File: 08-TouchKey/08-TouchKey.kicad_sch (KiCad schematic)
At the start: 21 parts, among them J1 AudioJack3, P1 TouchPaddles, P2 TouchPaddles, P3 TouchPaddles, P4 TouchPaddles, P5 TouchPaddles, P6 TouchPaddles, Q1 Q_Dual_PMOS_S1G1D2S2G2D1, U1 AT42QT1011-TSHR, U2 AT42QT1011-TSHR

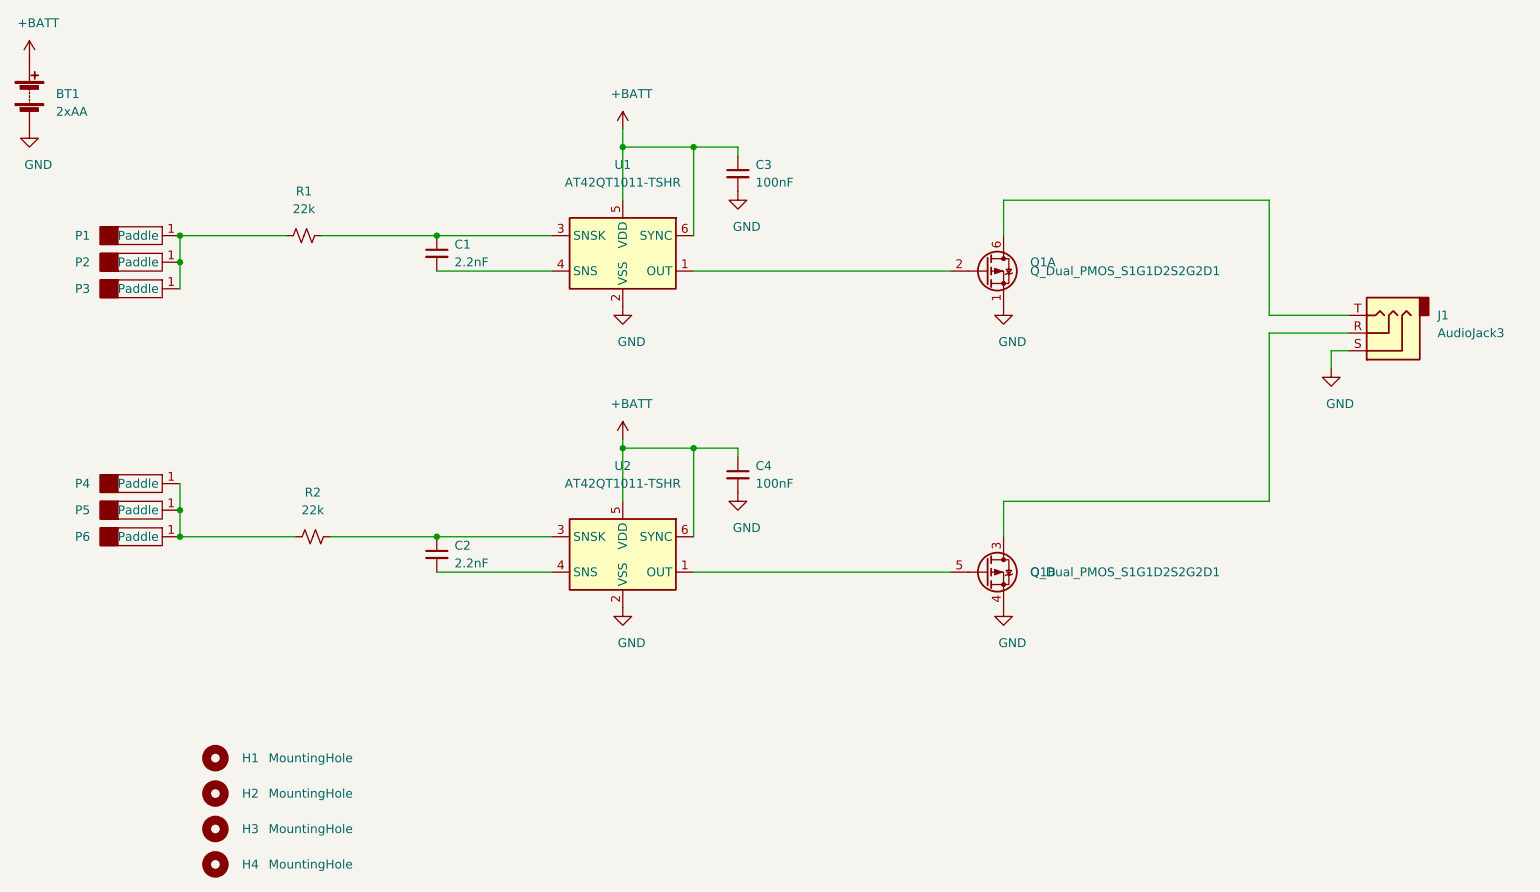
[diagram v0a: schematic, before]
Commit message: Update key and paddle to add more solder pads to improve mounting
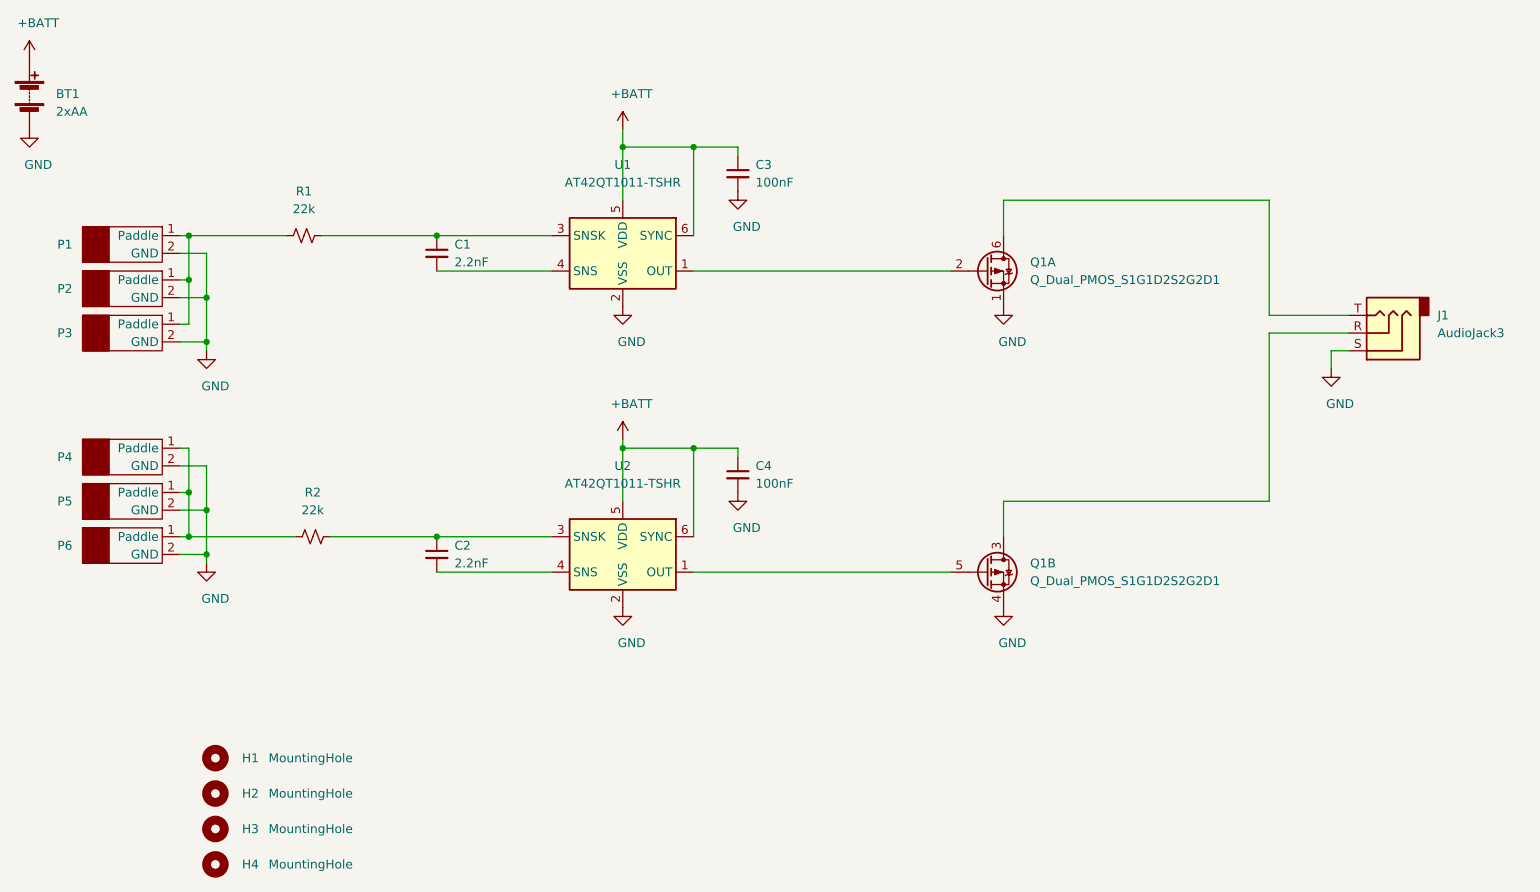
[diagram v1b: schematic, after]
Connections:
- net GND: now also P1.2 (GND), P2.2 (GND), P3.2 (GND), P4.2 (GND), P5.2 (GND), P6.2 (GND)
